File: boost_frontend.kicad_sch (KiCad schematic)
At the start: 23 parts, among them U1 LT8342RV-TRMPBF

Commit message: Working on layout for dev board
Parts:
- R1: value 33.6k -> 31.6k; Mfr KOA Speer Electronics, Inc. -> Susumu; Mfr P/N RN73R1JTTD3362B25 -> RG1608P-3162-B-T5; Supplier_1 P/N 2019-RN73R1JTTD3362B25TR-ND -> RG16P31.6KBTR-ND; Supplier_1 Unit Price 0.04314 -> 0.10000
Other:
- note added: "5V regulator characteristics"
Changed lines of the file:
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@@
 		(members "EN" "PGOOD" "FB")
+	)
+	(text "5V regulator characteristics"
+		(exclude_from_sim no)
+		(at 64.77 156.21 0)
+		(effects
+			(font
+				(size 1.27 1.27)
+				(thickness 0.254)
+				(bold yes)
+			)
+		)
 	)
 	(text "Control scheme"
 		(exclude_from_sim no)
-		(at 95.25 163.83 0)
+		(at 106.426 156.21 0)
 		(effects
 			(font
@@
 	(text "Compensation network"
 		(exclude_from_sim no)
-		(at 60.96 163.83 0)
+		(at 61.468 173.99 0)
 		(effects
 			(font
@@
 	(text_box "R: 60.4k\nC: 3.3nF"
 		(exclude_from_sim no)
-		(at 50.546 165.354 0)
-		(size 25.4 5.08)
+		(at 51.054 175.26 0)
+		(size 36.83 5.08)
+		(margins 0.9525 0.9525 0.9525 0.9525)
+		(stroke
+			(width 0)
+			(type solid)
+		)
+		(fill
+			(type none)
+		)
+		(effects
+			(font
+				(size 1.27 1.27)
+				(thickness 0.1588)
+			)
+			(justify left top)
+		)
+	)
+	(text_box "Feedback pin is modulated by a I2C controlled digipot which is controlled by the MCU."
+		(exclude_from_sim no)
+		(at 109.22 49.53 0)
+		(size 15.24 17.78)
+		(margins 0.9525 0.9525 0.9525 0.9525)
+		(stroke
+			(width 0)
+			(type solid)
+		)
+		(fill
+			(type none)
+		)
+		(effects
+			(font
+				(size 1.27 1.27)
+				(thickness 0.1588)
+			)
+			(justify left top)
+		)
+	)
+	(text_box "Input filter from datasheet"
+		(exclude_from_sim no)
+		(at 45.72 96.52 0)
+		(size 30.48 3.81)
+		(margins 0.9525 0.9525 0.9525 0.9525)
+		(stroke
+			(width 0)
+			(type solid)
+		)
+		(fill
+			(type none)
+		)
+		(effects
+			(font
+				(size 1.27 1.27)
+				(thickness 0.1588)
+			)
+			(justify left top)
+		)
+	)
+	(text_box "Max current: 9A\nF_sw = 1.0 Mhz"
+		(exclude_from_sim no)
+		(at 51.308 157.48 0)
+		(size 36.83 8.89)
+		(margins 0.9525 0.9525 0.9525 0.9525)
+		(stroke
+			(width 0)
+			(type solid)
+		)
+		(fill
+			(type none)
+		)
+		(effects
+			(font
+				(size 1.27 1.27)
+			)
+			(justify left top)
+		)
+	)
+	(text_box "Output filter from datasheet"
+		(exclude_from_sim no)
+		(at 220.98 69.85 0)
+		(size 30.48 3.81)
 		(margins 0.9525 0.9525 0.9525 0.9525)
 		(stroke
@@
 		)
 	)
+	(polyline
+		(pts
+			(xy 116.84 67.31) (xy 116.84 71.12)
+		)
+		(stroke
+			(width 0)
+			(type default)
+		)
+	)
 	(wire
 		(pts
@@
 		(pts
 			(xy 60.96 104.14) (xy 71.12 104.14)
+		)
+		(stroke
+			(width 0)
+			(type default)
+		)
+	)
+	(polyline
+		(pts
+			(xy 116.84 71.12) (xy 121.92 76.2)
 		)
 		(stroke
@@
 			(table_cell "VSET1"
 				(exclude_from_sim no)
-				(at 88.138 165.354 0)
+				(at 99.314 157.734 0)
 				(size 19.05 2.54)
 				(margins 0.9525 0.9525 0.9525 0.9525)
@@
 			(table_cell "VSET2/FB"
 				(exclude_from_sim no)
-				(at 107.188 165.354 0)
+				(at 118.364 157.734 0)
 				(size 12.7 2.54)
 				(margins 0.9525 0.9525 0.9525 0.9525)
@@
 			(table_cell "Target VOUT"
 				(exclude_from_sim no)
-				(at 119.888 165.354 0)
+				(at 131.064 157.734 0)
 				(size 22.86 2.54)
 				(margins 0.9525 0.9525 0.9525 0.9525)
@@
 			(table_cell "100kΩ to INTVCC"
 				(exclude_from_sim no)
-				(at 88.138 167.894 0)
+				(at 99.314 160.274 0)
 				(size 19.05 2.54)
 				(margins 0.9525 0.9525 0.9525 0.9525)
@@
 			(table_cell "FB"
 				(exclude_from_sim no)
-				(at 107.188 167.894 0)
+				(at 118.364 160.274 0)
 				(size 12.7 2.54)
 				(margins 0.9525 0.9525 0.9525 0.9525)
@@
 			(table_cell "External Feedback"
 				(exclude_from_sim no)
-				(at 119.888 167.894 0)
+				(at 131.064 160.274 0)
 				(size 22.86 2.54)
 				(margins 0.9525 0.9525 0.9525 0.9525)
@@
 			)
 		)
-		(property "Value" "33.6k"
+		(property "Value" "31.6k"
 			(at 60.96 53.34 90)
 			(effects
@@
 			)
 		)
-		(property "Datasheet" "https://www.koaspeer.com/pdfs/RN73R.pdf"
+		(property "Datasheet" "https://mm.digikey.com/Volume0/opasdata/d220001/medias/docus/1162/RG_RM_RGH_Oct2012.pdf"
 			(at 60.96 55.88 0)
 			(effects
@@
 			)
 		)
-		(property "Description" "RES 33.6K OHM 0.1% 1/10W 0603"
+		(property "Description" "RES SMD 31.6KOHM 0.1% 1/10W 0603"
 			(at 60.96 55.88 0)
 			(effects
@@
 			)
 		)
-		(property "Mfr" "KOA Speer Electronics, Inc."
+		(property "Mfr" "Susumu"
 			(at 60.96 55.88 0)
 			(effects
@@
 			)
 		)
-		(property "Mfr P/N" "RN73R1JTTD3362B25"
+		(property "Mfr P/N" "RG1608P-3162-B-T5"
 			(at 60.96 55.88 0)
 			(effects
@@
 			)
 		)
-		(property "Supplier_1 P/N" "2019-RN73R1JTTD3362B25TR-ND"
+		(property "Supplier_1 P/N" "RG16P31.6KBTR-ND"
 			(at 60.96 55.88 0)
 			(effects
@@
 			)
 		)
-		(property "Supplier_1 Unit Price" "0.04314"
+		(property "Supplier_1 Unit Price" "0.10000"
 			(at 60.96 55.88 0)
 			(effects

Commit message: Move
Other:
- note added: "Boost characteristics"
- note removed: "5V regulator characteristics"
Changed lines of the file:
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@@
 		(members "EN" "PGOOD" "FB")
 	)
-	(text "5V regulator characteristics"
+	(text "Boost characteristics"
 		(exclude_from_sim no)
 		(at 64.77 156.21 0)

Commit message: Fixing circuit errors
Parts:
- L1: footprint _Power_Board:IND_SER2918H-333KL -> _PowerBoard:IND_SER2918H-333KL
- U1: footprint _Power_Board:05-08-7040_ADI -> _PowerBoard:05-08-7040_ADI
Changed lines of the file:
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@@
 			)
 		)
-		(property "Footprint" "_Power_Board:IND_SER2918H-333KL"
+		(property "Footprint" "_PowerBoard:IND_SER2918H-333KL"
 			(at 151.13 128.27 0)
 			(effects
@@
 			)
 		)
-		(property "Footprint" "_Power_Board:05-08-7040_ADI"
+		(property "Footprint" "_PowerBoard:05-08-7040_ADI"
 			(at 176.53 109.22 0)
 			(effects

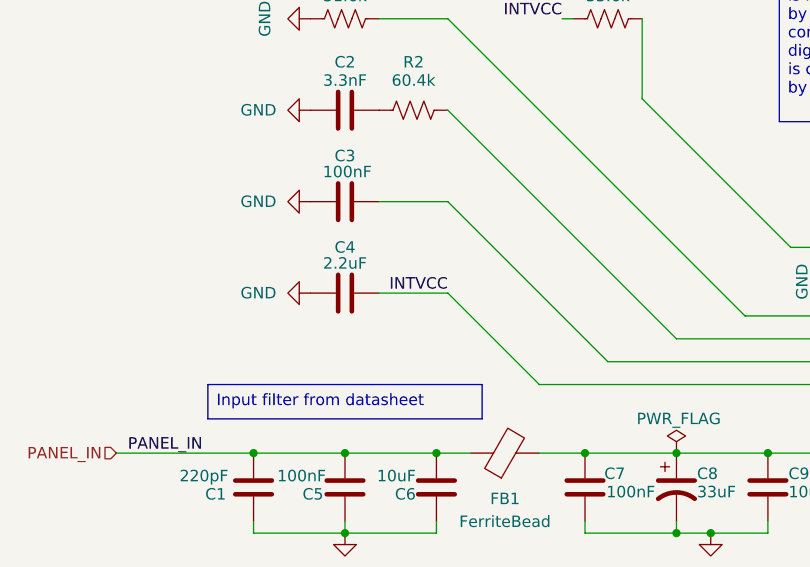
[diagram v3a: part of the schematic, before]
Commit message: Most of frontend layout done. Still need to add in power and analog ground
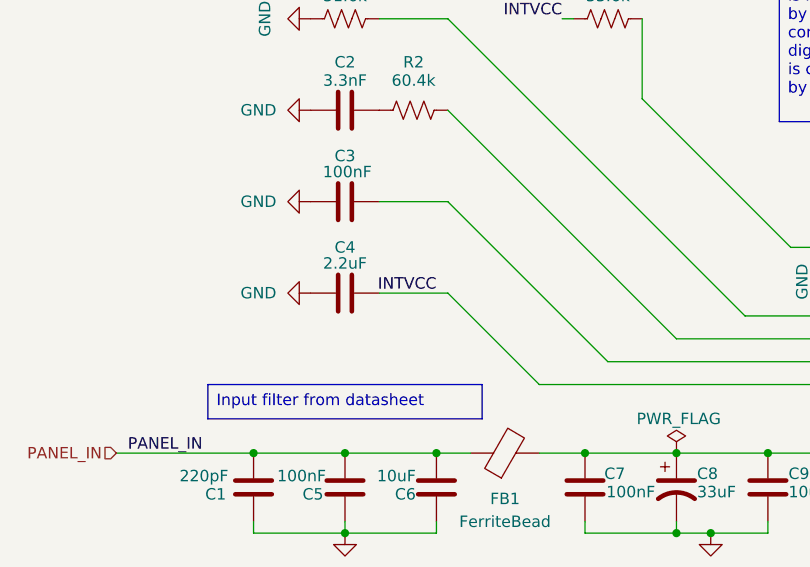
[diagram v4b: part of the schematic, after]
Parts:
- L1: footprint _PowerBoard:IND_SER2918H-333KL -> _PowerBoard:IND_XGL1313_COC; Mfr P/N SER2918H-333KL -> XGL1313-333MED; Supplier_1 Digikey -> Coilcraft; Supplier_1 P/N 2457-SER2918H-333KL-ND -> XGL1313-333MED; Supplier_1 Unit Price 6.98000 -> 6.83000
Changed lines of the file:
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@@
 	)
 	(label "INTVCC"
-		(at 72.39 86.36 180)
+		(at 71.12 86.36 180)
 		(effects
 			(font
@@
 			)
 		)
-		(property "Footprint" "_PowerBoard:IND_SER2918H-333KL"
+		(property "Footprint" "_PowerBoard:IND_XGL1313_COC"
 			(at 151.13 128.27 0)
 			(effects
@@
 			)
 		)
-		(property "Datasheet" "https://www.coilcraft.com/getmedia/a2805f49-c9b8-42c0-9939-b2d75eed7288/ser2900.pdf"
+		(property "Datasheet" "https://www.coilcraft.com/getmedia/755c440a-d891-4d48-aaf8-866731f65aab/xgl1313.pdf"
 			(at 151.13 128.27 0)
 			(effects
@@
 			)
 		)
-		(property "Mfr P/N" "SER2918H-333KL"
+		(property "Mfr P/N" "XGL1313-333MED"
 			(at 151.13 128.27 0)
 			(effects
@@
 			)
 		)
-		(property "Supplier_1" "Digikey"
+		(property "Supplier_1" "Coilcraft"
 			(at 151.13 128.27 0)
 			(effects
@@
 			)
 		)
-		(property "Supplier_1 P/N" "2457-SER2918H-333KL-ND"
+		(property "Supplier_1 P/N" "XGL1313-333MED"
 			(at 151.13 128.27 0)
 			(effects
@@
 			)
 		)
-		(property "Supplier_1 Unit Price" "6.98000"
+		(property "Supplier_1 Unit Price" "6.83000"
 			(at 151.13 128.27 0)
 			(effects
